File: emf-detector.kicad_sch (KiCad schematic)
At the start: 32 parts

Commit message: Add EMF Circuit
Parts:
- added C? (x2): 2.2uF, symbol Device:C
- added C?: C, symbol Device:C
- added C?: 2.2K, symbol Device:C
- added D? (x11): LED, symbol Device:LED
- added L? (x2): 100mH, symbol Device:L
- added R?: R, symbol Device:R
- added R? (x2): 1K, symbol Device:R
- added R?: 10k, symbol Device:R
- added RV?: R_Potentiometer, symbol Device:R_Potentiometer
- added U?: LM358, symbol Amplifier_Operational:LM358
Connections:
- net GND: now also J?.S, U?.3 (+)
- net at RV?.1: now also RV?.2, R?.2
- net at RV?.3: now also U?.1, C?.1
- net at U?.2 (-): now also R?.1, R?.2
- net at U?.3 (+): now also L?.1, L?.2
- net at J?.R: now also C?.2
- net at J?.T: now also C?.2
- new net: C?.2, R?.1 (x2)
- new net: C?.1, L?.1
- new net: C?.1, L?.2
- new net: R?.1, R?.2, U?.2 (-)
- new net: R?.2, RV?.1, RV?.2
- new net: C?.1, RV?.3, U?.1
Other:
- note added: "Electromagnetic Field Detection (EMF) Circuit"
- moved on the sheet: BT?, J?, RV?, U?, U?A

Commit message: Update 7-Segment Diplay and LED Display Driver
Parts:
- removed U?: LTC-4627JR, Display_7Segment:LTC-4627Jx, symbol Display_Character:LTC-4627JR
- added R?: 10K, symbol Device:R
- added U?: MAX7219CWG+T, 21-0042B_24_MXM, symbol emf-detector-library-3:MAX7219CWG+T
- added U?: TDCR1060M, TDCG1060M_VIS, symbol emf-detector-library:TDCR1060M
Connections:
- net +5V: now also U?.19 (V+)
- net GND: now also R?.2, U?.4 (GND), U?.9 (GND)
- net LOAD: now reaches U?.10 (IO5)
- net LOAD: now also U?.12 (LOAD)
- net CLK: now reaches U?.24 (IO18)
- net CLK: now also U?.13 (CLK)
- net DIN: now reaches U?.25 (IO19)
- net DIN: now also U?.1 (DIN)
- new net: R?.1, U?.18 (ISET)
- new net DIGIT_1: U?.1, U?.2 (DIG_0)
- new net DIGIT_2: U?.11 (DIG_1), U?.12
- new net DIGIT_3: U?.10, U?.6 (DIG_2)
- new net DIGIT_4: U?.4, U?.7 (DIG_3)
- new net SEG_A: U?.11, U?.14 (SEG_A)
- new net SEG_B: U?.16 (SEG_B), U?.8
- new net SEG_C: U?.20 (SEG_C), U?.5
- new net SEG_D: U?.23 (SEG_D), U?.3
- new net SEG_DP: U?.22 (SEG_DP), U?.6
- new net SEG_E: U?.2, U?.21 (SEG_E)
- new net SEG_F: U?.15 (SEG_F), U?.9
- new net SEG_G: U?.17 (SEG_G), U?.7
- no-connect marks 27 -> 33
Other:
- note added: "7-Segment, 4-Digit LED Display"
- note added: "LED Display Driver"

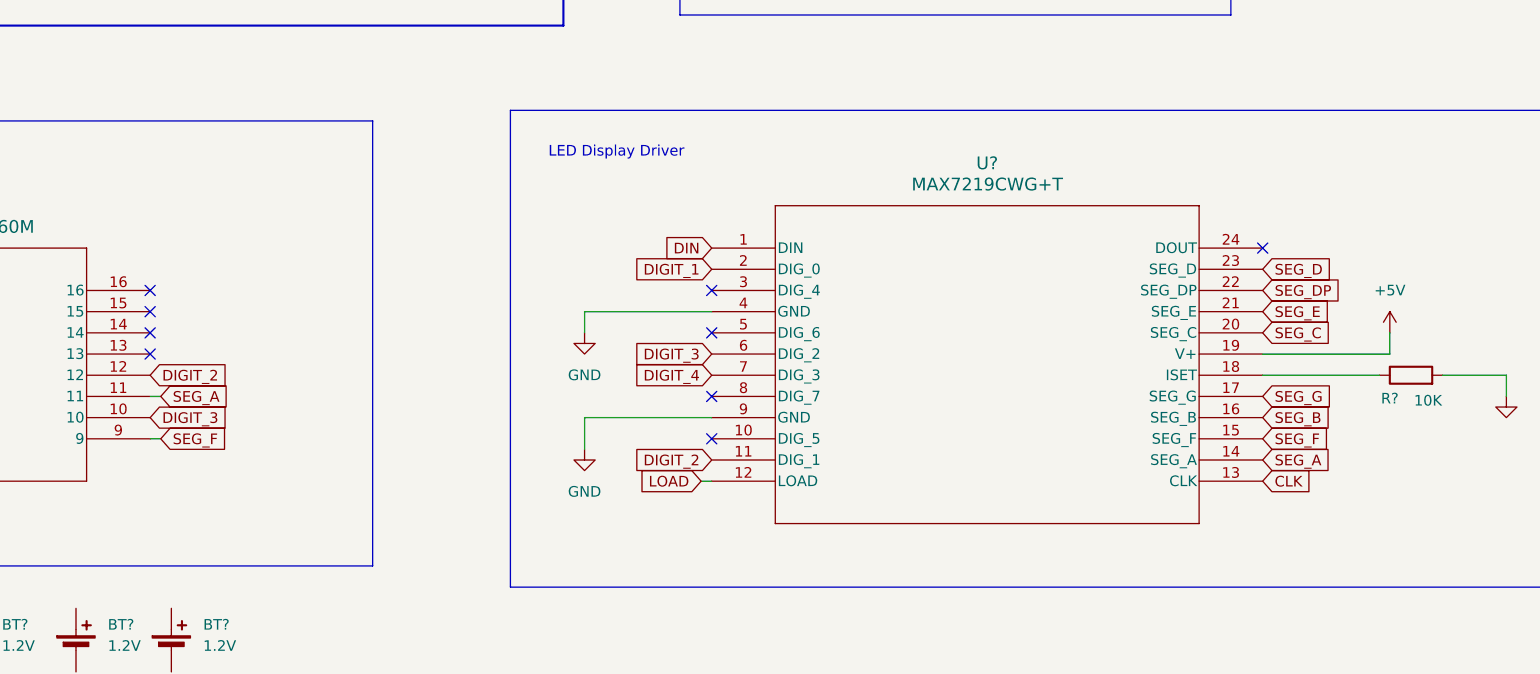
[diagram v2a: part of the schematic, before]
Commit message: Rename symbols and footprints
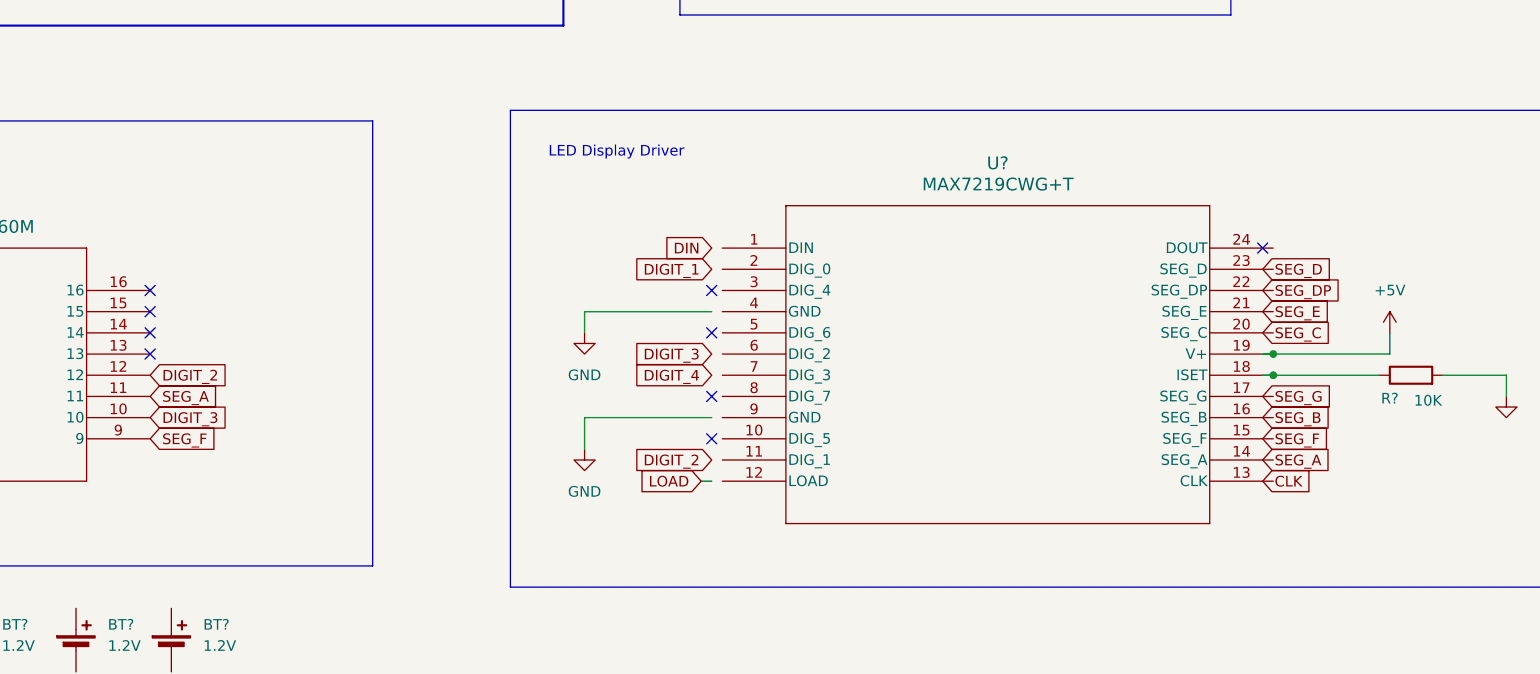
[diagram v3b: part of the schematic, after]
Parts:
- removed U?: MAX7219CWG+T, 21-0042B_24_MXM, symbol emf-detector-library-3:MAX7219CWG+T
- removed U?: TDCR1060M, TDCG1060M_VIS, symbol emf-detector-library:TDCR1060M
- added U?: MAX7219CWG+T, 21-0042B_24_MXM, symbol emf-detector-library-3:MAX7219CWG+T
- added U?: TDCR1060M, TDCG1060M_VIS, symbol emf-detector-library-1:TDCR1060M
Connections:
- net +5V: now also U?.19 (V+)
- net DIGIT_1: now also U?.1
- net DIGIT_2: now also U?.12
- net DIGIT_3: now also U?.10
- net DIGIT_4: now also U?.4
- net SEG_A: now also U?.11
- net SEG_B: now also U?.8
- net SEG_C: now also U?.5
- net SEG_D: now also U?.3
- net SEG_DP: now also U?.6
- net SEG_E: now also U?.2
- net SEG_F: now also U?.9
- net SEG_G: now also U?.7
- net at R?.1: now also U?.18 (ISET)

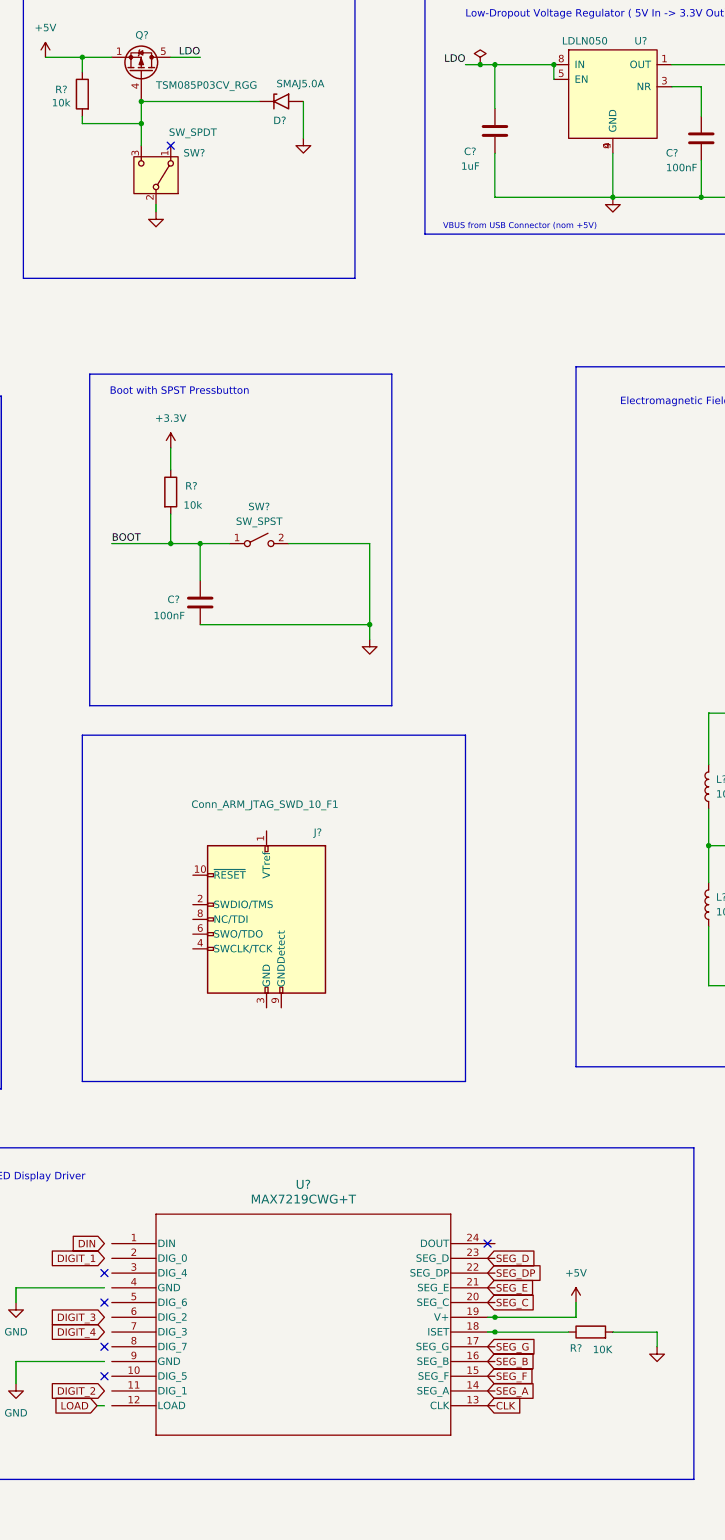
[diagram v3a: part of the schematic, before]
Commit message: Rename symbols and footprints
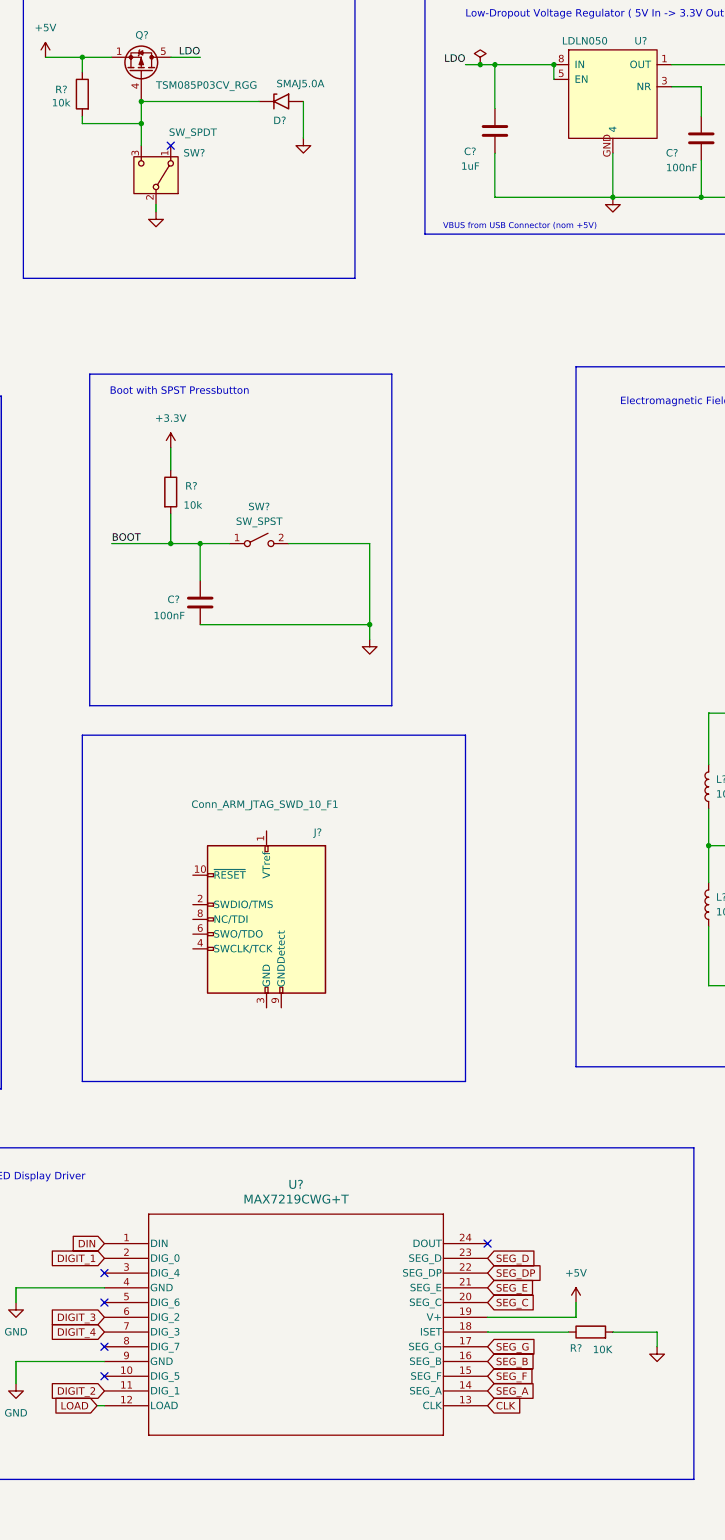
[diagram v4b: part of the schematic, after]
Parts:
- removed U?: MAX7219CWG+T, 21-0042B_24_MXM, symbol emf-detector-library-3:MAX7219CWG+T
- removed U?: TDCR1060M, TDCG1060M_VIS, symbol emf-detector-library-1:TDCR1060M
- added U?: TDCR1060M, TDCG1060M_VIS, symbol emf-detector-library-4:TDCR1060M
- added U?: MAX7219CWG+T, 21-0042B_24_MXM, symbol emf-detector-library-6:MAX7219CWG+T
- Q?: footprint JITTER-COMPONENTS:PDFN33-1EP_3x3mm_P0.65mm -> Jitter_IC:PDFN33-1EP_3x3mm_P0.65mm
- U?: footprint F1-LED-CIRCUIT-LIBRARY:SON_2XV6T1G_ONS -> sot:SOT-563
- U?: footprint Darko:ESP32C6MINI1N4 -> (none)
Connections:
- net +5V: now also U?.19 (V+)
- net CLK: now also U?.13 (CLK)
- net DIGIT_1: now also U?.1, U?.2 (DIG_0)
- net DIGIT_2: now also U?.11 (DIG_1), U?.12
- net DIGIT_3: now also U?.10, U?.6 (DIG_2)
- net DIGIT_4: now also U?.4, U?.7 (DIG_3)
- net DIN: now also U?.1 (DIN)
- net GND: now also U?.GND (4), U?.4 (GND), U?.9 (GND); no longer U?.4 (GND), U?.9 (GND)
- net LOAD: now also U?.12 (LOAD)
- net SEG_A: now also U?.11, U?.14 (SEG_A)
- net SEG_B: now also U?.16 (SEG_B), U?.8
- net SEG_C: now also U?.20 (SEG_C), U?.5
- net SEG_D: now also U?.23 (SEG_D), U?.3
- net SEG_DP: now also U?.22 (SEG_DP), U?.6
- net SEG_E: now also U?.2, U?.21 (SEG_E)
- net SEG_F: now also U?.15 (SEG_F), U?.9
- net SEG_G: now also U?.17 (SEG_G), U?.7
- net at R?.1: now also U?.18 (ISET)

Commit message: Update README.md
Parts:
- removed D?: LED, symbol Device:LED
- removed J?: Conn_ARM_JTAG_SWD_10_F1, F1-LED-CIRCUIT-LIBRARY:SAMTEC_FTSH-105-XX-X-DV, symbol F1-LED-CIRCUIT-LIBRARY:Conn_ARM_JTAG_SWD_10_F1
- added D?: SD03, Darko:SOD323, symbol Diode:SMAJ5.0A
- added J?: TC2030-MCP, TC2030MCP, symbol Darko:TC2030-MCP
- added R? (x10): 1K 0402, Resistor_SMD:R_0402_1005Metric, symbol Device:R_Small
- added U?: DRV5053RAQLPG, LPG3_TEX, symbol emf-detector-library-5:DRV5053RAQLPG
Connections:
- net +3V3: now also D?.1 (A1), J?.2
- net +5V: now also U?.1 (VCC)
- net BOOT: now also J?.6
- net EN: now also J?.1
- net GND: now also D?.1 (K), D?.1 (K), D?.1 (K), D?.1 (K), D?.1 (K), D?.1 (K), D?.1 (K), D?.1 (K), D?.1 (K), D?.1 (K), D?.2 (A2), J?.4, U?.2 (GND)
- net LED_8: now reaches D?.2 (A)
- net LED_8: now also R?.1
- net LED_3: now reaches D?.2 (A)
- net LED_3: now also R?.1
- net at U?.15 (IO6): now also R?.2
- net at U?.16 (IO7): now also R?.2
- net at U?.17 (IO12): now also R?.2
- net at U?.18 (IO13): now also R?.2
- net at U?.19 (IO14): now also R?.2
- net at U?.20 (IO15): now also R?.2
- net at U?.26 (IO20): now also R?.2
- net at U?.27 (IO21): now also R?.2
- net at U?.28 (IO22): now also R?.2
- net at U?.29 (IO23): now also R?.2
- net RXD0: now reaches U?.30 (RXD0)
- net RXD0: now also J?.5
- net TXD0: now reaches U?.31 (TXD0)
- net TXD0: now also J?.3
- net ADC1_CH0: now reaches U?.9 (IO4)
- net ADC1_CH0: now also U?.3 (OUT)
- net LED_2: now reaches D?.2 (A)
- net LED_2: now also R?.1
- net LED_1: now reaches D?.2 (A)
- net LED_1: now also R?.1
- net LED_6: now reaches D?.2 (A)
- net LED_6: now also R?.1
- net LED_4: now reaches D?.2 (A)
- net LED_4: now also R?.1
- net LED_7: now reaches D?.2 (A)
- net LED_7: now also R?.1
- net LED_5: now reaches D?.2 (A)
- net LED_5: now also R?.1
- net LED_9: now reaches D?.2 (A)
- net LED_9: now also R?.1
- net LED_10: now reaches D?.2 (A)
- net LED_10: now also R?.1
- no-connect marks 33 -> 20
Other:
- note added: "Hall Sensor"
- note added: "LED Indicators"
- moved on the sheet: BT?, D?
